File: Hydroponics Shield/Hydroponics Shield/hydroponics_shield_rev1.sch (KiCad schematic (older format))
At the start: 50 parts, among them CON1 BARREL_JACK, J1 282836-6, J2 282836-6, P1 CONN_01X02, P2 CONN_01X03, P3 CONN_01X04, P4 CONN_01X02, P5 CONN_01X02, P9 0731000105, Q1 2N7000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

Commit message: desktop night changes
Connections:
- net +5V: now also PCB1.5 (VCC)
- net DOSING_PUMP_1: now also SHIELD1.10; no longer SHIELD1.11
- net DOSING_PUMP_2: now also SHIELD1.9; no longer SHIELD1.10
- net GND: now also PCB1.4 (GND)
- net LED_STRIP_OUT: now also SHIELD1.11; no longer SHIELD1.6
- net MAIN_PUMP: now also SHIELD1.6; no longer SHIELD1.9
- net at R10.2, R9.1: now also PCB1.3 (TX)
- net at Q4.1 (S), R7.1: now also PCB1.2 (RX)
- net Vguard: now reaches P9.2 (SHIELD1), P9.3 (SHIELD2), U1.1, U1.2 (-)
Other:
- moved on the sheet: PCB1
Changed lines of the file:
@@
 Text GLabel 8250 4950 0    50   Input ~ 0
 LED_STRIP_OUT
-Text GLabel 3150 1800 2    50   Input ~ 0
+Text GLabel 3150 1200 2    50   Input ~ 0
 LED_STRIP_OUT
 Text GLabel 3150 2300 2    50   Input ~ 0
@@
 	9750 3200 9750 3150
 Connection ~ 9750 3150
-Text GLabel 3150 1200 2    50   Input ~ 0
+Text GLabel 3150 1300 2    50   Input ~ 0
 DOSING_PUMP_1
-Text GLabel 3150 1300 2    50   Input ~ 0
+Text GLabel 3150 1400 2    50   Input ~ 0
 DOSING_PUMP_2
-Text GLabel 3150 1400 2    50   Input ~ 0
+Text GLabel 3150 1800 2    50   Input ~ 0
 MAIN_PUMP
 Wire Wire Line
@@
 L HC05_BLUETOOTH PCB1
 U 1 1 5AEEC53B
-P 6900 1550
-F 0 "PCB1" H 6925 1100 60  0000 C CNN
-F 1 "HC05_BLUETOOTH" H 6925 1975 60  0000 C CNN
-F 2 "USER_MODULES:HC05_BLUETOOTH_SMD" H 6825 1000 60  0001 C CNN
-F 3 "" H 6900 1550 60  0000 C CNN
-	1    6900 1550
+P 6925 1550
+F 0 "PCB1" H 6950 1100 60  0000 C CNN
+F 1 "HC05_BLUETOOTH" H 6950 1975 60  0000 C CNN
+F 2 "USER_MODULES:HC05_BLUETOOTH_SMD" H 6850 1000 60  0001 C CNN
+F 3 "" H 6925 1550 60  0000 C CNN
+	1    6925 1550
 	-1   0    0    -1
 $EndComp
 NoConn ~ 6500 1400
 NoConn ~ 6500 1700
+Text GLabel 3950 6550 2    60   Input ~ 0
+Vguard
+Wire Wire Line
+	3900 6550 3950 6550
+Connection ~ 3900 6550
 $EndSCHEMATC

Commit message: workday additions
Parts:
- CON1: value BARREL_JACK -> PJ-202A
- P1, P4, P5: value CONN_01X02 -> 22-05-3021
- P2: value CONN_01X03 -> 0022053031
- P3: value CONN_01X04 -> 0022053041
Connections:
- net PH_VREF is gone; now on net PH_VOUT: SHIELD1.AD1
- net +12V: now also J1.1, J1.2, J1.3
- net GND: no longer J1.1, J1.2, J1.3
- net PH_VOUT: no longer SHIELD1.AD0
- net TEMP_SENSE_IN: now also SHIELD1.AD0; no longer SHIELD1.AD2
- net Vguard: now also SHIELD1.AD2
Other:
- note added: "Barrel jack is 2.1mmx5.5mm\nCompatible supply could be:\nSDI65-12-UDC-P5R (this is likely overkill, we could probably use a cheaper one)"
- note added: "POWER BUDGET:\nWorst Case 12V input:\nLED Strips:\nSearches put them somewhere near 0.5A per 5 foot strip\nWe have space for 3, including safety factor, budget for 2A total.\n\nMotors: Worst case 1.75A total\n\n4A/48W worst case continuous current consumption (with safety factor)\n"
- moved on the sheet: J1
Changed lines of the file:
@@
 	-1   0    0    -1
 $EndComp
-Text GLabel 1150 1900 0    50   Input ~ 0
+Text GLabel 1150 2000 0    50   Input ~ 0
 PH_VOUT
-Text GLabel 1150 2000 0    50   Input ~ 0
-PH_VREF
 Text Notes 875  2875 0    50   ~ 0
 +12V IN
@@
 P 7150 4700
 F 0 "P3" H 7150 4950 50  0000 C CNN
-F 1 "CONN_01X04" V 7250 4700 50  0000 C CNN
+F 1 "0022053041" V 7250 4700 50  0000 C CNN
 F 2 "Pin_Headers:Pin_Header_Angled_1x04" H 7150 4700 50  0001 C CNN
 F 3 "" H 7150 4700 50  0000 C CNN
@@
 Text Notes 2350 2850 0    50   ~ 0
 can use MCP9700\nor similar
-Text GLabel 1150 2100 0    50   Input ~ 0
+Text GLabel 1150 1900 0    50   Input ~ 0
 TEMP_SENSE_IN
 Text Notes -2200 7000 0    50   ~ 0
@@
 P 900 3250
 F 0 "CON1" H 900 3500 50  0000 C CNN
-F 1 "BARREL_JACK" H 900 3050 50  0000 C CNN
+F 1 "PJ-202A" H 900 3050 50  0000 C CNN
 F 2 "Connect:BARREL_JACK" H 900 3250 50  0001 C CNN
 F 3 "" H 900 3250 50  0000 C CNN
@@
 	1    0    0    -1
 $EndComp
-Wire Wire Line
-	8900 4500 9700 4500
-Wire Wire Line
-	8900 5250 9700 5250
 Connection ~ 8900 5250
 Wire Wire Line
-	9600 4500 9600 4800
-Wire Wire Line
-	9600 4800 9700 4800
-Connection ~ 9600 4500
-Wire Wire Line
-	9600 4950 9600 5250
-Wire Wire Line
-	9600 4950 9700 4950
-Connection ~ 9600 5250
-Wire Wire Line
-	9600 4650 9700 4650
-Connection ~ 9600 4650
-Wire Wire Line
-	9600 5100 9700 5100
-Connection ~ 9600 5100
-Text Notes 9450 4350 0    60   ~ 0
+	9550 5100 9550 5400
+Wire Wire Line
+	9550 5400 9650 5400
+Wire Wire Line
+	9550 5250 9650 5250
+Connection ~ 9550 5250
+Text Notes 10100 5100 0    60   ~ 0
 GROW LIGHTS OUT
 Text Notes 10700 850  0    60   ~ 0
@@
 L 282836-6 J1
 U 1 1 5AEDA89B
-P 9750 4850
-F 0 "J1" H 9725 5125 60  0000 C CNN
-F 1 "282836-6" H 9725 5050 60  0000 C CNN
-F 2 "USER_CONNECTORS:282836-6" H 9650 5225 60  0001 C CNN
-F 3 "" H 9750 4950 60  0001 C CNN
-	1    9750 4850
-	0    1    -1   0
+P 9700 5050
+F 0 "J1" H 9675 5325 60  0000 C CNN
+F 1 "282836-6" H 9675 5250 60  0000 C CNN
+F 2 "USER_CONNECTORS:282836-6" H 9600 5425 60  0001 C CNN
+F 3 "" H 9700 5150 60  0001 C CNN
+	1    9700 5050
+	0    1    1    0
 $EndComp
 $Comp
@@
 P 800 4300
 F 0 "P1" H 800 4450 50  0000 C CNN
-F 1 "CONN_01X02" V 900 4300 50  0000 C CNN
+F 1 "22-05-3021" V 900 4300 50  0000 C CNN
 F 2 "Pin_Headers:Pin_Header_Angled_1x02" H 800 4300 50  0001 C CNN
 F 3 "" H 800 4300 50  0000 C CNN
@@
 P 2150 4300
 F 0 "P4" H 2150 4450 50  0000 C CNN
-F 1 "CONN_01X02" V 2250 4300 50  0000 C CNN
+F 1 "22-05-3021" V 2250 4300 50  0000 C CNN
 F 2 "Pin_Headers:Pin_Header_Angled_1x02" H 2150 4300 50  0001 C CNN
 F 3 "" H 2150 4300 50  0000 C CNN
@@
 P 800 5150
 F 0 "P2" H 800 5350 50  0000 C CNN
-F 1 "CONN_01X03" V 900 5150 50  0000 C CNN
+F 1 "0022053031" V 900 5150 50  0000 C CNN
 F 2 "Pin_Headers:Pin_Header_Angled_1x03" H 800 5150 50  0001 C CNN
 F 3 "" H 800 5150 50  0000 C CNN
@@
 P 3550 4300
 F 0 "P5" H 3550 4450 50  0000 C CNN
-F 1 "CONN_01X02" V 3650 4300 50  0000 C CNN
+F 1 "22-05-3021" V 3650 4300 50  0000 C CNN
 F 2 "Pin_Headers:Pin_Header_Angled_1x02" H 3550 4300 50  0001 C CNN
 F 3 "" H 3550 4300 50  0000 C CNN
@@
 	3900 6550 3950 6550
 Connection ~ 3900 6550
+Text Notes -3850 3700 0    60   ~ 0
+POWER BUDGET:\nWorst Case 12V input:\nLED Strips:\nSearches put them somewhere near 0.5A per 5 foot strip\nWe have space for 3, including safety factor, budget for 2A total.\n\nMotors: Worst case 1.75A total\n\n4A/48W worst case continuous current consumption (with safety factor)\n
+Text Notes -3850 2700 0    60   ~ 0
+Barrel jack is 2.1mmx5.5mm\nCompatible supply could be:\nSDI65-12-UDC-P5R (this is likely overkill, we could probably use a cheaper one)
+Text GLabel 1150 2100 0    50   Input ~ 0
+Vguard
+Wire Wire Line
+	8900 4500 9250 4500
+Wire Wire Line
+	9250 4500 9250 5100
+Wire Wire Line
+	9250 5100 9650 5100
+Connection ~ 9550 5100
+Wire Wire Line
+	9550 4950 9650 4950
+Wire Wire Line
+	9550 4450 9550 4950
+Wire Wire Line
+	9550 4650 9650 4650
+Wire Wire Line
+	9650 4800 9550 4800
+Connection ~ 9550 4800
+$Comp
+L +12V #PWR038
+U 1 1 5AED1397
+P 9550 4450
+F 0 "#PWR038" H 9550 4300 50  0001 C CNN
+F 1 "+12V" H 9550 4590 50  0000 C CNN
+F 2 "" H 9550 4450 50  0000 C CNN
+F 3 "" H 9550 4450 50  0000 C CNN
+	1    9550 4450
+	1    0    0    -1
+$EndComp
+Connection ~ 9550 4650
 $EndSCHEMATC

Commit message: changes made extra pump wifi
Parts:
- removed PCB1: HC05_BLUETOOTH, USER_MODULES:HC05_BLUETOOTH_SMD, symbol HC05_BLUETOOTH
- added C6: 5ZLH100MEFC6.3X11, Capacitors_ThroughHole:C_Radial_D6.3_L11.2_P2.5, symbol 5ZLH100MEFC6.3X11
- added D4: 1N4148, Diodes_ThroughHole:Diode_DO-35_SOD27_Horizontal_RM10, symbol 1N4148
- added PCB1: ESP8266, USER_MODULES:ESP8266, symbol ESP8266
- added Q9: PSMN022-30PL,127, TO_SOT_Packages_THT:TO-220_Neutral123_Horizontal_LargePads, symbol PSMN022-30PL,127
- added R22: 10.0k, Resistors_ThroughHole:Resistor_Horizontal_RM10mm, symbol R
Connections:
- net +12V: now also J1.6, SHIELD1.V_IN, C6.1, D4.1 (K); no longer J1.3
- net +3V3: now also PCB1.4 (CHPD), PCB1.8 (3V3)
- net GND: now also SHIELD1.GND3, PCB1.1 (GND), Q9.3 (S), R22.1
- net MAIN_PUMP: now also SHIELD1.12; no longer SHIELD1.6
- net at R10.2, R9.1: now also PCB1.7 (RXI)
- net at Q4.1 (S), R7.1: now also PCB1.2 (TXO)
- net at J1.4, Q5.2 (D): now also J1.3; no longer J1.5, J1.6
- net BLE_DATA_RECEIVE renamed WIFI_DATA_RECEIVE
- net BLE_DATA_TRANSMIT renamed WIFI_DATA_TRANSMIT
- new net: C6.2, D4.2 (A), J1.5, Q9.2 (D)
- new net TOPUP_PUMP: Q9.1 (G), R22.2, SHIELD1.6
- no-connect marks 2 -> 0
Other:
- moved on the sheet: J1, Q5, R11

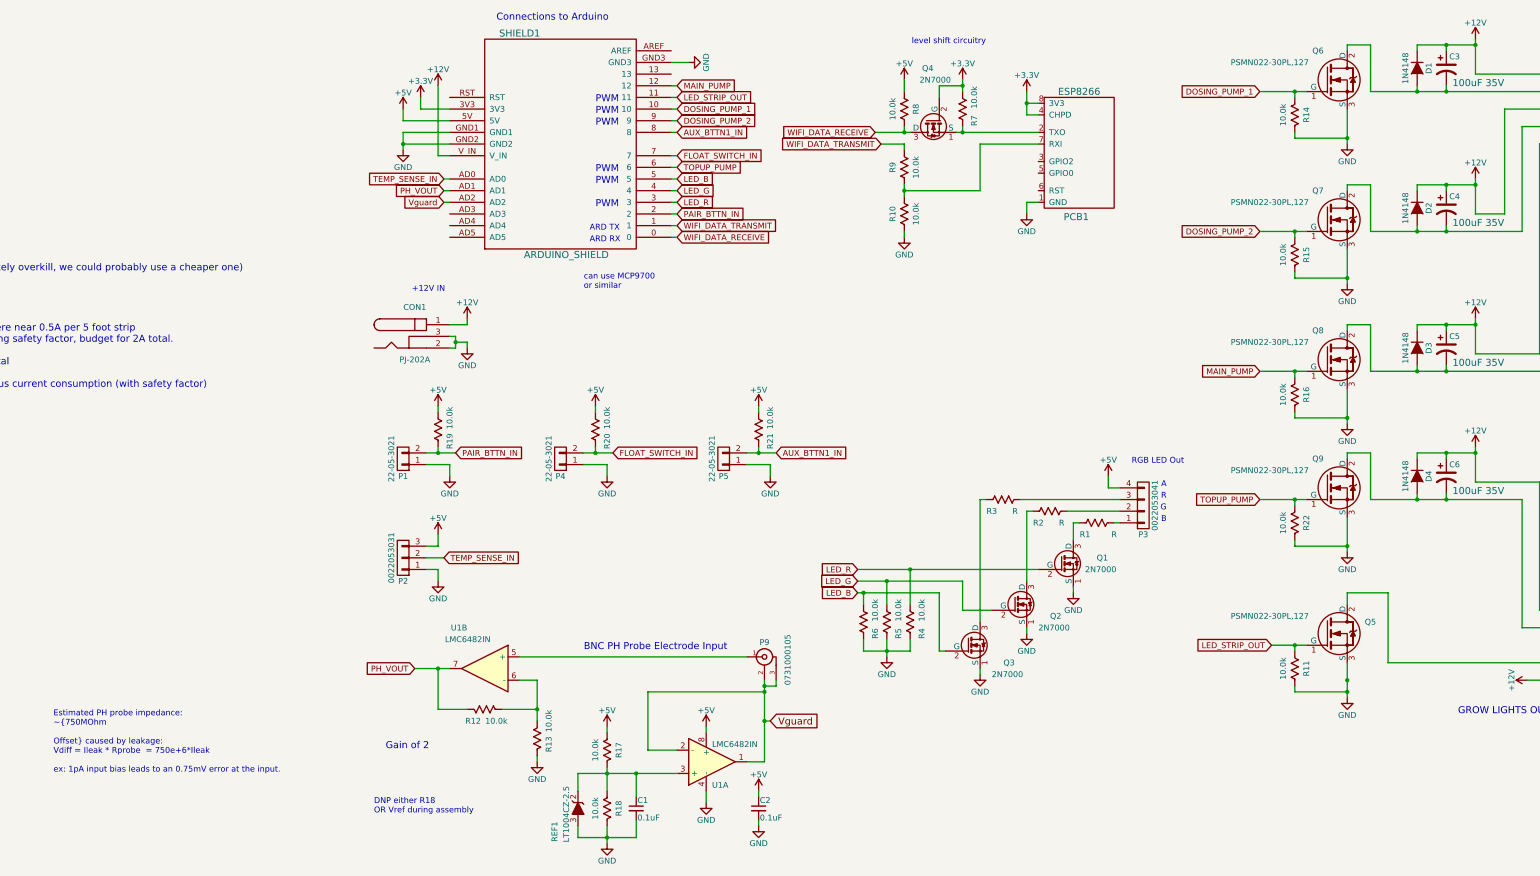
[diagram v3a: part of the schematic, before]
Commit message: finished board change from bt to wifi
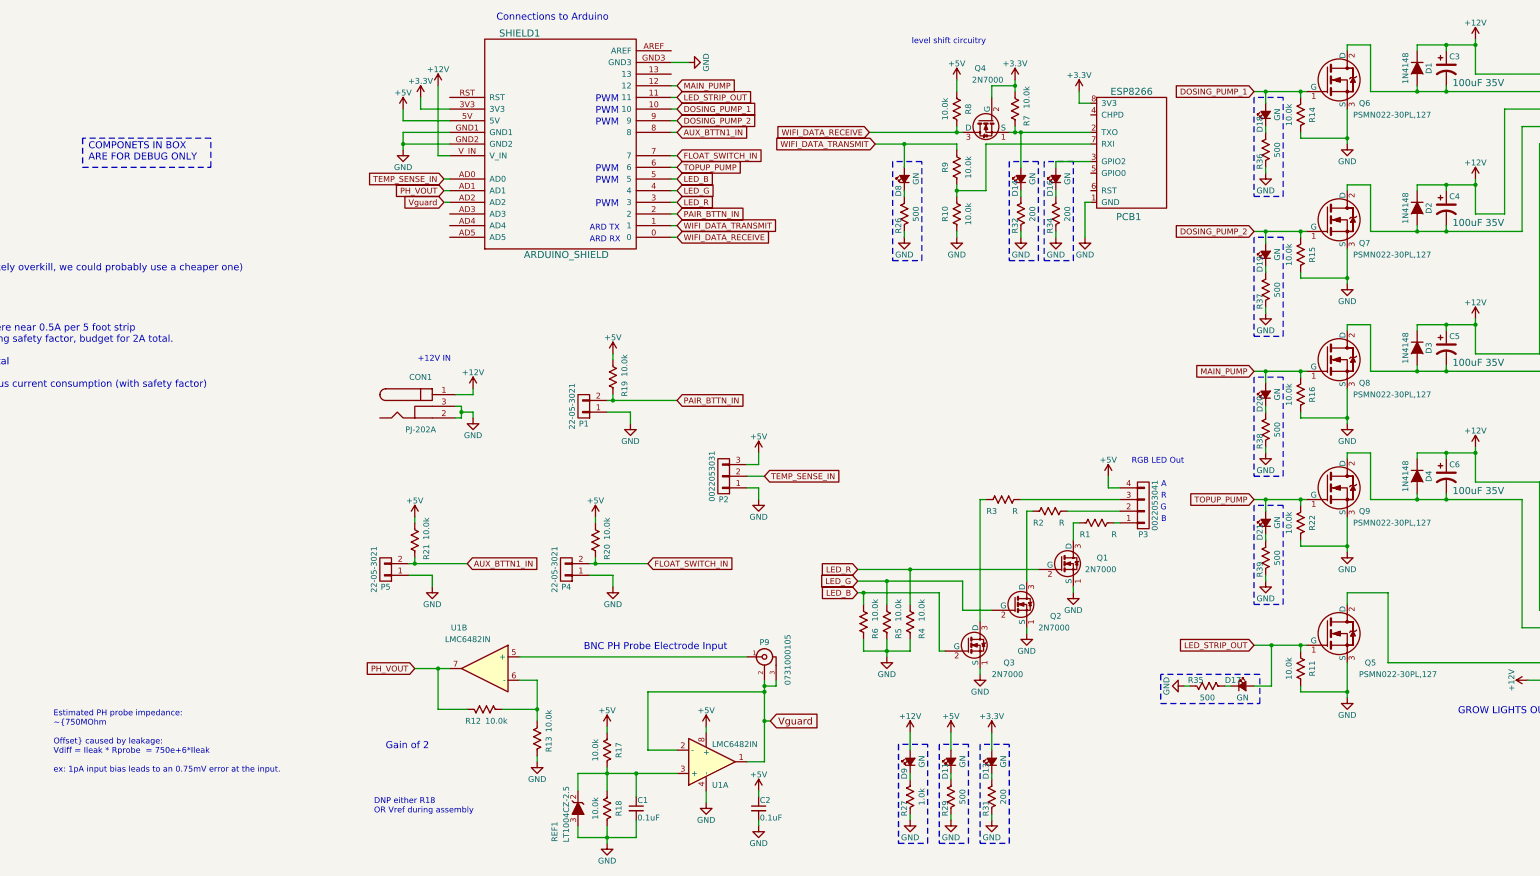
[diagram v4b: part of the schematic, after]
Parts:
- added D11, D13, D14, D16, D17, D18, D19, D20, D21, D8, D9: GN, LEDs:LED_0805, symbol Led_Small
- added R26, R29, R35, R36, R37, R38, R39: 500, Resistors_SMD:R_0805_HandSoldering, symbol R
- added R27: 1.0k, Resistors_SMD:R_0805_HandSoldering, symbol R
- added R31, R32, R34: 200, Resistors_SMD:R_0805_HandSoldering, symbol R
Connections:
- net +12V: now also D9.2 (A)
- net +3V3: now also D13.2 (A); no longer PCB1.4 (CHPD)
- net +5V: now also D11.2 (A)
- net DOSING_PUMP_1: now also D18.2 (A)
- net DOSING_PUMP_2: now also D19.2 (A)
- net GND: now also R26.2, R27.2, R29.2, R31.2, R32.2, R34.2, R35.2, R36.2, R37.2, R38.2, R39.2
- net LED_STRIP_OUT: now also D17.2 (A)
- net MAIN_PUMP: now also D20.2 (A)
- net TOPUP_PUMP: now also D21.2 (A)
- net WIFI_DATA_TRANSMIT: now also D8.2 (A)
- net at PCB1.2 (TXO), Q4.1 (S), R7.1: now also D14.2 (A)
- net at PCB1.3 (GPIO2): now also D16.2 (A)
- new net: D8.1 (K), R26.1
- new net: D14.1 (K), R32.1
- new net: D18.1 (K), R36.1
- new net: D19.1 (K), R37.1
- new net: D20.1 (K), R38.1
- new net: D21.1 (K), R39.1
- new net: D17.1 (K), R35.1
- new net: D11.1 (K), R29.1
- new net: D13.1 (K), R31.1
- new net: D9.1 (K), R27.1
- new net: D16.1 (K), R34.1
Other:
- note added: "COMPONETS IN BOX \nARE FOR DEBUG ONLY"
- note removed: "can use MCP9700\nor similar"
- moved on the sheet: CON1, P1, P2, P4, P5, PCB1, Q4, R10, R11, R14, R15, R16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
